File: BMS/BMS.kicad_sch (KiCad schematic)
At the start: 6 parts, among them IC1 STM32H742VIT6

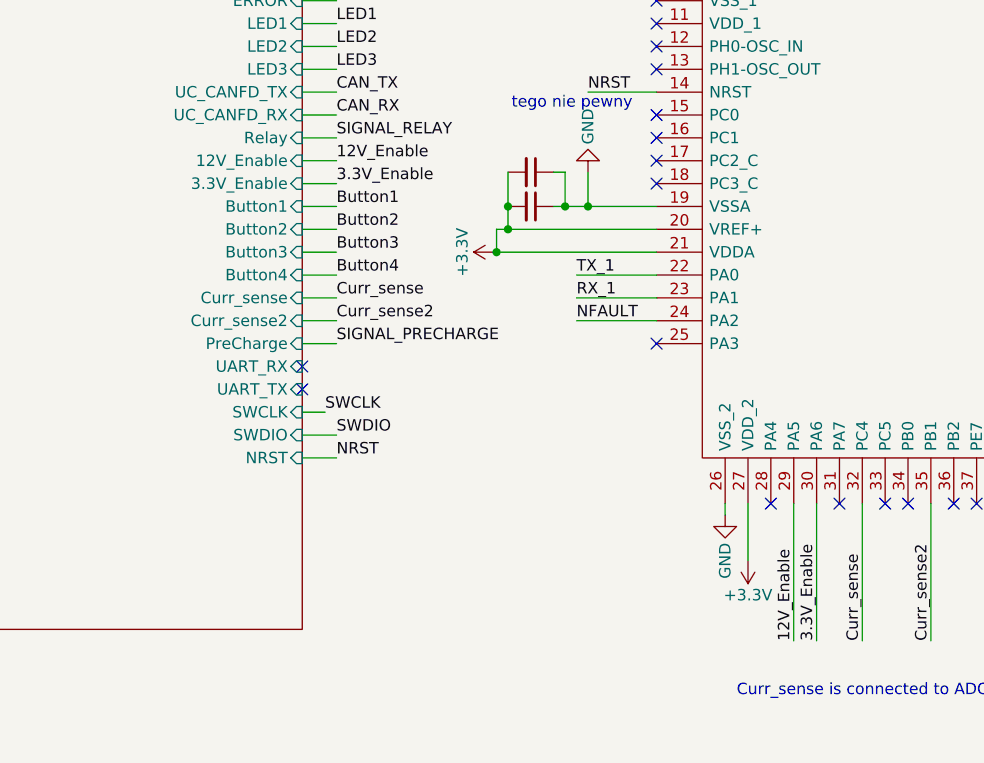
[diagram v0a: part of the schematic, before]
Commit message: Dodano layout drugiego bq79614, ukladu tlumaczącego z protokułu TI na UART oraz wstępnie poprowadzono pary różnicowe
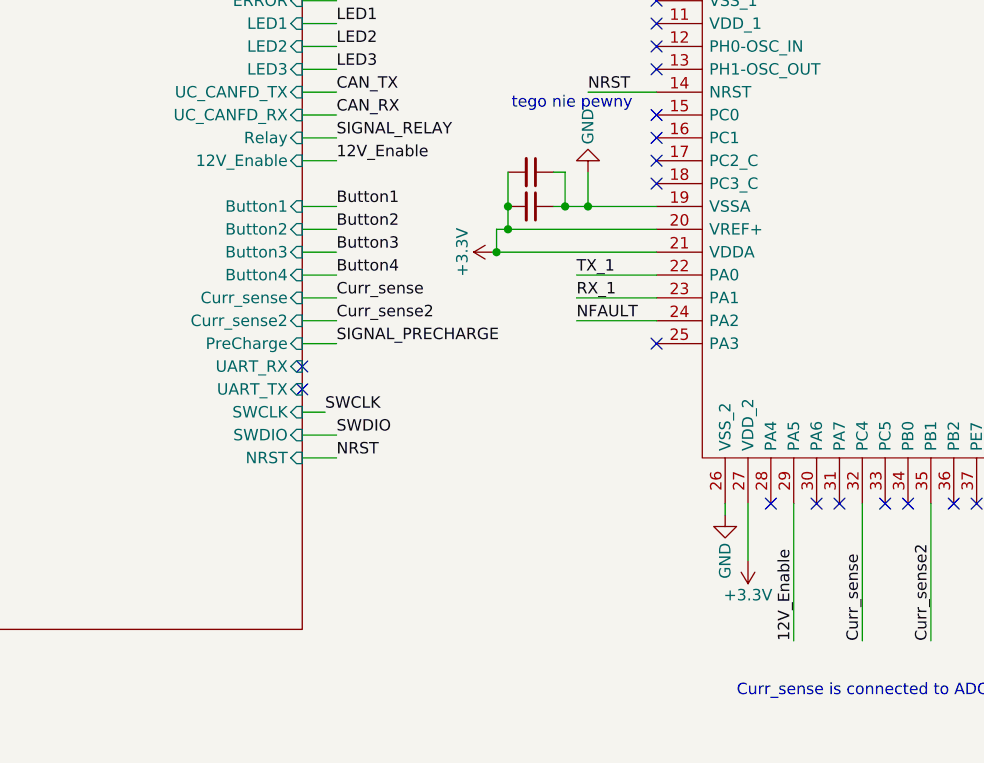
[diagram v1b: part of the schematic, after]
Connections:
- net 3.3V_Enable: no longer names the net of IC1.30 (PA6)
- no-connect marks 61 -> 62
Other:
- sheet Connectivity ports: added none; removed 3.3V_Enable
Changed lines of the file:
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@@
 	)
 	(no_connect
+		(at 137.16 133.35)
+	)
+	(no_connect
 		(at 119.38 74.93)
 	)
@@
 	(wire
 		(pts
-			(xy 80.01 97.79) (xy 83.82 97.79)
-		)
-		(stroke
-			(width 0)
-			(type default)
-		)
-	)
-	(wire
-		(pts
 			(xy 226.06 95.25) (xy 226.06 82.55)
 		)
@@
 	(wire
 		(pts
-			(xy 137.16 133.35) (xy 137.16 148.59)
-		)
-		(stroke
-			(width 0)
-			(type default)
-		)
-	)
-	(wire
-		(pts
 			(xy 111.76 87.63) (xy 119.38 87.63)
 		)
@@
 		)
 	)
-	(label "3.3V_Enable"
-		(at 83.82 97.79 0)
-		(fields_autoplaced yes)
-		(effects
-			(font
-				(size 1.27 1.27)
-			)
-			(justify left bottom)
-		)
-	)
 	(label "12V_Enable"
 		(at 134.62 148.59 90)
@@
 		)
 	)
-	(label "3.3V_Enable"
-		(at 137.16 148.59 90)
-		(fields_autoplaced yes)
-		(effects
-			(font
-				(size 1.27 1.27)
-			)
-			(justify left bottom)
-		)
-	)
 	(label "SWCLK"
 		(at 187.96 25.4 270)
@@
 			(effects
 				(font
-					(size 1.27 1.27)
-				)
-				(justify right)
-			)
-		)
-		(pin "3.3V_Enable" input
-			(at 80.01 97.79 0)
-			(effects
-				(font

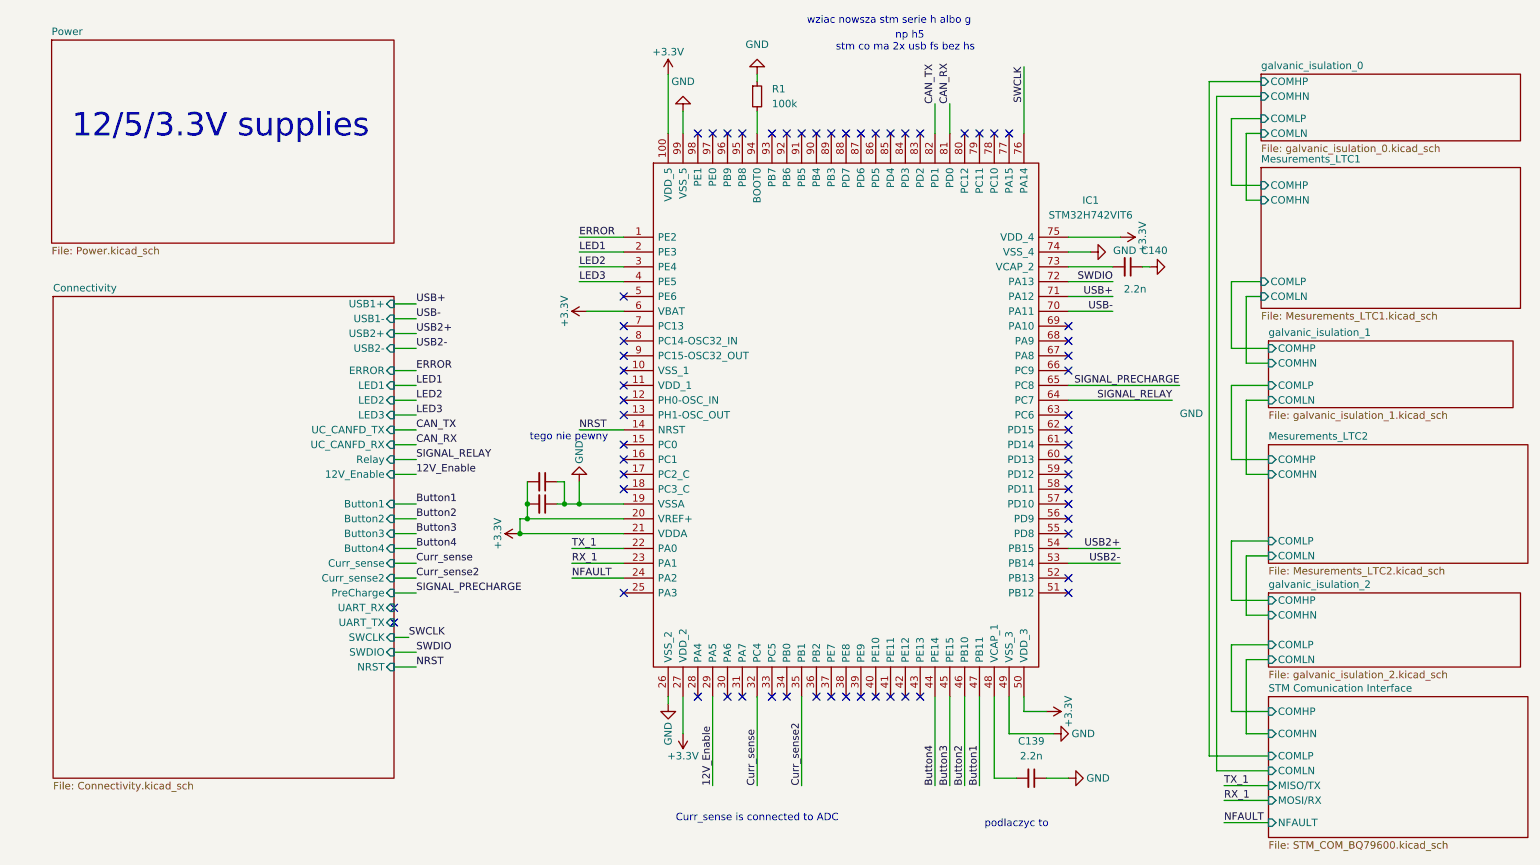
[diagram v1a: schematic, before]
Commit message: Iteracja 1.0 gotowa, teraz sprawdzenie i zmiany kosmetyczne
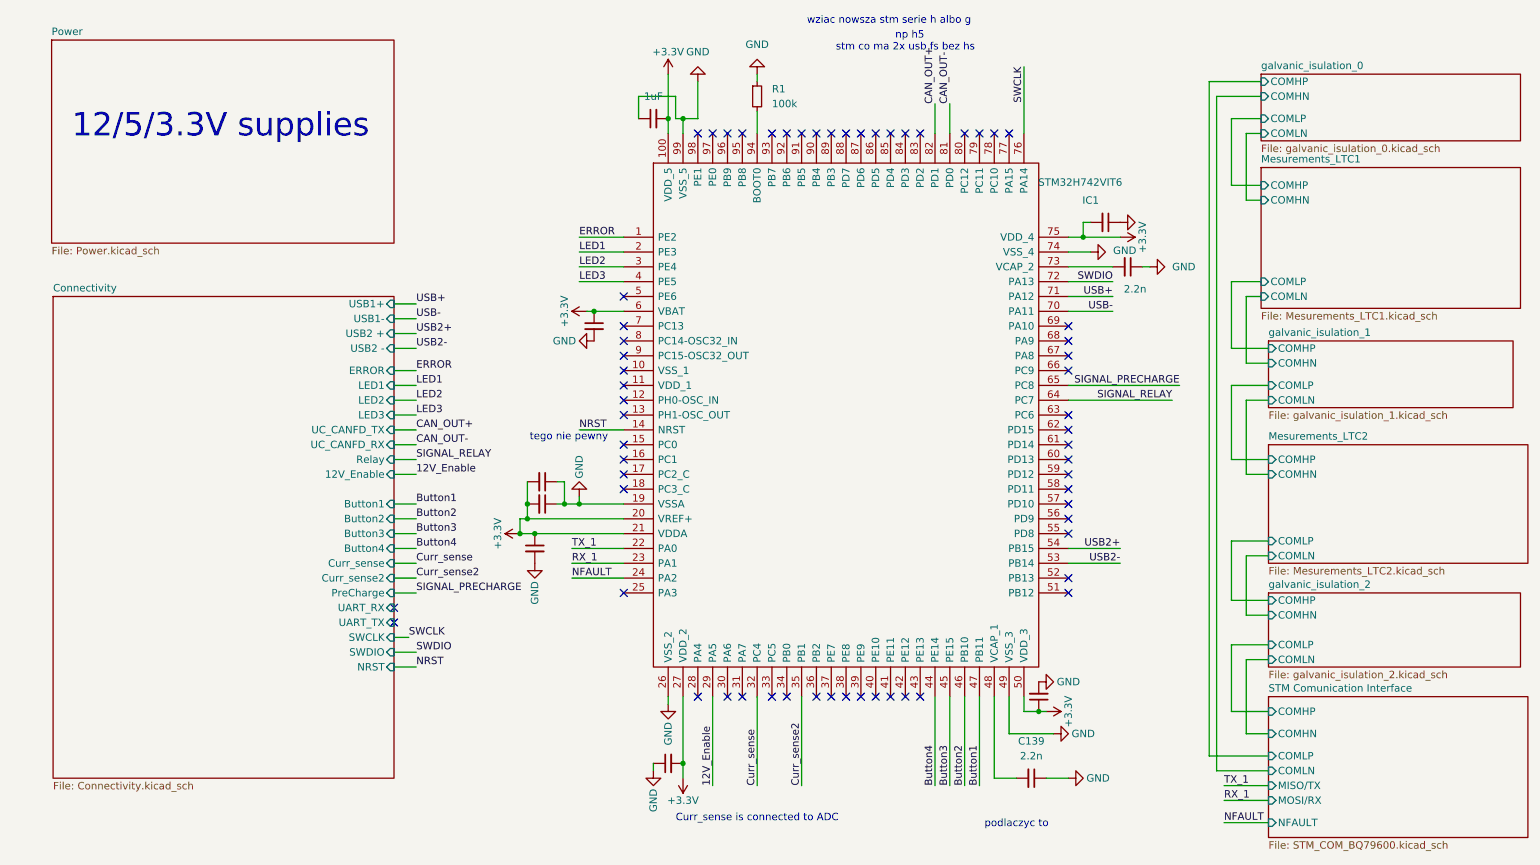
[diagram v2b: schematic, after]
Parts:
- added C65, C66, C67, C68, C69, C70: 1uF, Capacitor_SMD:C_0603_1608Metric_Pad1.08x0.95mm_HandSolder, symbol Device:C_Small
- C141: value 47n -> 47n
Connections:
- net +3.3V: now also C65.2, C66.1, C67.2, C68.1, C69.2, C70.1
- net GND: now also C65.1, C66.2, C67.1, C68.2, C69.1, C70.2
- net CAN_RX renamed CAN_OUT-
- net CAN_TX renamed CAN_OUT+
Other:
- sheet Connectivity ports: added USB2 +, USB2 -; removed USB2+, USB2-
